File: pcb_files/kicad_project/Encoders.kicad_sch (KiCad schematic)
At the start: 10 parts, among them IC1 AS5145B-HSST, IC2 AS5145B-HSST

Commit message: Finaliza (En principio) el esquematico
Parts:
- removed ENC_1_DAT_CONN1, ENC_2_DAT_CONN1: Conn_01x03_Male, PCB_ZoroBot_v3:Placa_Dat_Encd_Zoro, symbol PCB_ZoroBot_v3-rescue:Conn_01x03_Male-Connector
- removed ENC_1_POT_CONN1, ENC_2_POT_CONN1: Conn_01x02_Male, PCB_ZoroBot_v3:Placa_Pot_Encd_Zoro, symbol PCB_ZoroBot_v3-rescue:Conn_01x02_Male-Connector
- added ENC_D_CONN, ENC_I_CONN: Conn_01x05_Pin, symbol Connector:Conn_01x05_Pin
- renumbered C35 to C23, C36 to C24, C37 to C25, C46 to C31, IC2 to ENC_D1, IC1 to ENC_I1
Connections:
- net ENC_1_3.3 renamed ENC_I_3.3
- net ENC_I_3.3: now also ENC_I_CONN.2 (Pin_2)
- net ENC_1_A_CONN renamed ENC_I_A_CONN
- net ENC_I_A_CONN: now also ENC_I_CONN.3 (Pin_3)
- net ENC_1_B_CONN renamed ENC_I_B_CONN
- net ENC_I_B_CONN: now also ENC_I_CONN.4 (Pin_4)
- net ENC_1_GND renamed ENC_I_GND
- net ENC_I_GND: now also ENC_I_CONN.1 (Pin_1)
- net ENC_1_I_CONN renamed ENC_I_I_CONN
- net ENC_I_I_CONN: now also ENC_I_CONN.5 (Pin_5)
- net ENC_2_3.3 renamed ENC_D_3.3
- net ENC_D_3.3: now also ENC_D_CONN.2 (Pin_2)
- net ENC_2_A_CONN renamed ENC_D_A_CONN
- net ENC_D_A_CONN: now also ENC_D_CONN.3 (Pin_3)
- net ENC_2_B_CONN renamed ENC_D_B_CONN
- net ENC_D_B_CONN: now also ENC_D_CONN.4 (Pin_4)
- net ENC_2_GND renamed ENC_D_GND
- net ENC_D_GND: now also ENC_D_CONN.1 (Pin_1)
- net ENC_2_I_CONN renamed ENC_D_I_CONN
- net ENC_D_I_CONN: now also ENC_D_CONN.5 (Pin_5)
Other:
- note added: "ENCODER MOTOR DERECHO"
- note added: "ENCODER MOTOR IZQUIERDO"
- moved on the sheet: C23, C24, C25, C31, ENC_D1, ENC_I1

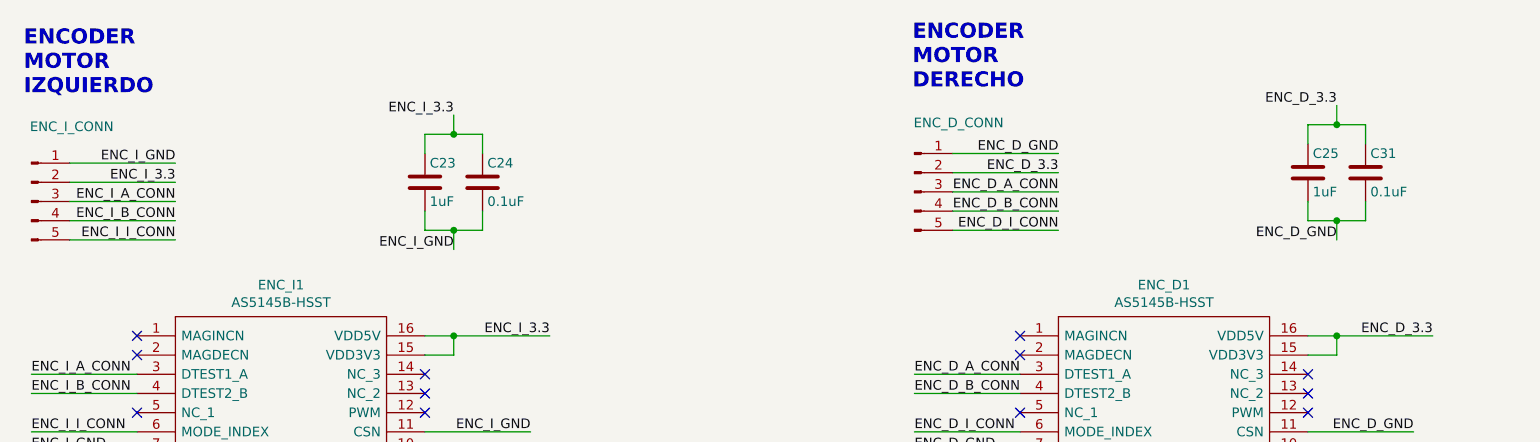
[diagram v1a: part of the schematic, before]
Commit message: Correlaciona toda la NetList, añade EdgeCuts y comienza el posicionamiento de componentes
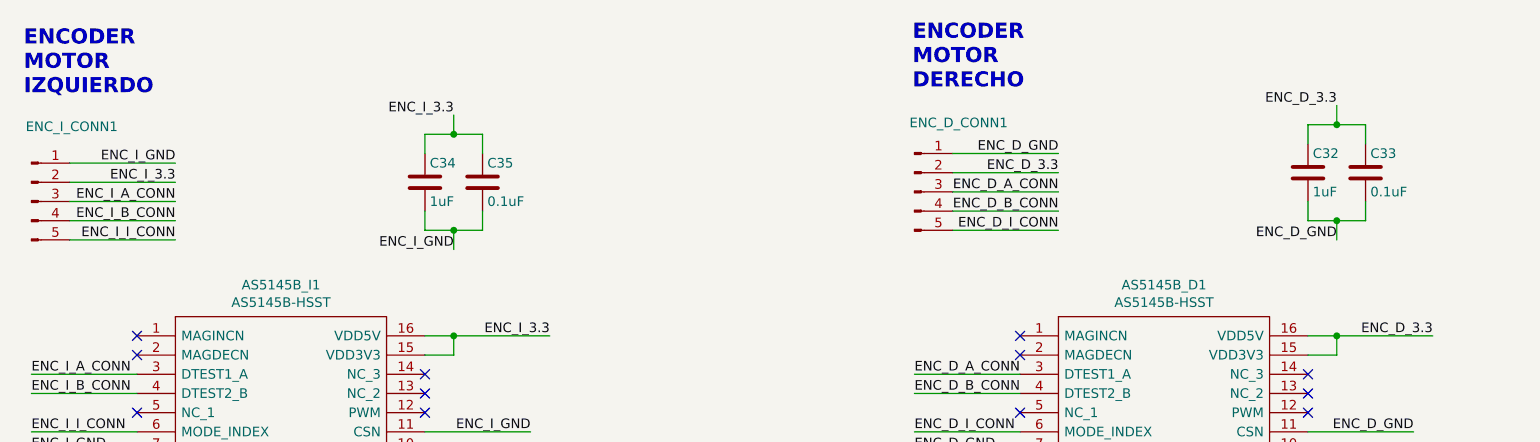
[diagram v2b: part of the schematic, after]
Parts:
- AS5145B_D1: renamed from ENC_D1; footprint AS5145B-HSST:SOP65P780X199-16N -> Package_SO:SSOP-16_5.3x6.2mm_P0.65mm
- AS5145B_I1: renamed from ENC_I1; footprint AS5145B-HSST:SOP65P780X199-16N -> Package_SO:SSOP-20_5.3x7.2mm_P0.65mm
- C32: renamed from C25; footprint Capacitor_SMD:C_0805_2012Metric -> Capacitor_SMD:C_0402_1005Metric_Pad0.74x0.62mm_HandSolder
- C33: renamed from C31; footprint Capacitor_SMD:C_0805_2012Metric -> Capacitor_SMD:C_0402_1005Metric_Pad0.74x0.62mm_HandSolder
- C34: renamed from C23; footprint Capacitor_SMD:C_0805_2012Metric -> Capacitor_SMD:C_0402_1005Metric_Pad0.74x0.62mm_HandSolder
- C35: renamed from C24; footprint Capacitor_SMD:C_0805_2012Metric -> Capacitor_SMD:C_0402_1005Metric_Pad0.74x0.62mm_HandSolder
- ENC_D_CONN1: renamed from ENC_D_CONN; footprint (none) -> custom_footprints:FujitoraBot2_PCBmodule_encoder
- ENC_I_CONN1: renamed from ENC_I_CONN; footprint (none) -> custom_footprints:FujitoraBot2_PCBmodule_encoder
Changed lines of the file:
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@@
 		(on_board yes)
 		(dnp no)
-		(property "Reference" "ENC_I_CONN"
+		(property "Reference" "ENC_I_CONN1"
 			(at 57.404 75.184 0)
 			(effects
@@
 			)
 		)
-		(property "Footprint" ""
+		(property "Footprint" "custom_footprints:FujitoraBot2_PCBmodule_encoder"
 			(at 52.07 85.09 0)
 			(effects
@@
 			(project ""
 				(path "/38e8b839-c362-4120-bbf7-582efa82e48d/fe1aa100-f33c-4fed-9a9a-b5cbbb3bba93"
-					(reference "ENC_I_CONN")
+					(reference "ENC_I_CONN1")
 					(unit 1)
 				)
@@
 		(on_board yes)
 		(dnp no)
-		(property "Reference" "C31"
+		(property "Reference" "C33"
 			(at 229.235 78.74 0)
 			(effects
@@
 			)
 		)
-		(property "Footprint" "Capacitor_SMD:C_0805_2012Metric"
+		(property "Footprint" "Capacitor_SMD:C_0402_1005Metric_Pad0.74x0.62mm_HandSolder"
 			(at 229.5652 85.09 0)
 			(effects
@@
 			(project "ZoroBot3"
 				(path "/38e8b839-c362-4120-bbf7-582efa82e48d/fe1aa100-f33c-4fed-9a9a-b5cbbb3bba93"
-					(reference "C31")
+					(reference "C33")
 					(unit 1)
 				)
@@
 		(on_board yes)
 		(dnp no)
-		(property "Reference" "ENC_I1"
+		(property "Reference" "AS5145B_I1"
 			(at 85.09 96.139 0)
 			(effects
@@
 			)
 		)
-		(property "Footprint" "AS5145B-HSST:SOP65P780X199-16N"
+		(property "Footprint" "Package_SO:SSOP-20_5.3x7.2mm_P0.65mm"
 			(at 100.33 100.33 0)
 			(effects
@@
 			(project "ZoroBot3"
 				(path "/38e8b839-c362-4120-bbf7-582efa82e48d/fe1aa100-f33c-4fed-9a9a-b5cbbb3bba93"
-					(reference "ENC_I1")
+					(reference "AS5145B_I1")
 					(unit 1)
 				)
@@
 		(on_board yes)
 		(dnp no)
-		(property "Reference" "C25"
+		(property "Reference" "C32"
 			(at 221.615 78.74 0)
 			(effects
@@
 			)
 		)
-		(property "Footprint" "Capacitor_SMD:C_0805_2012Metric"
+		(property "Footprint" "Capacitor_SMD:C_0402_1005Metric_Pad0.74x0.62mm_HandSolder"
 			(at 221.9452 85.09 0)
 			(effects
@@
 			(project "ZoroBot3"
 				(path "/38e8b839-c362-4120-bbf7-582efa82e48d/fe1aa100-f33c-4fed-9a9a-b5cbbb3bba93"
-					(reference "C25")
+					(reference "C32")
 					(unit 1)
 				)
@@
 		(on_board yes)
 		(dnp no)
-		(property "Reference" "ENC_D1"
+		(property "Reference" "AS5145B_D1"
 			(at 201.93 96.139 0)
 			(effects
@@
 			)
 		)
-		(property "Footprint" "AS5145B-HSST:SOP65P780X199-16N"
+		(property "Footprint" "Package_SO:SSOP-16_5.3x6.2mm_P0.65mm"
 			(at 217.17 100.33 0)
 			(effects
@@
 			(project "ZoroBot3"
 				(path "/38e8b839-c362-4120-bbf7-582efa82e48d/fe1aa100-f33c-4fed-9a9a-b5cbbb3bba93"
-					(reference "ENC_D1")
+					(reference "AS5145B_D1")
 					(unit 1)
 				)
@@
 		(on_board yes)
 		(dnp no)
-		(property "Reference" "ENC_D_CONN"
+		(property "Reference" "ENC_D_CONN1"
 			(at 174.752 74.676 0)
 			(effects
@@
 			)
 		)
-		(property "Footprint" ""
+		(property "Footprint" "custom_footprints:FujitoraBot2_PCBmodule_encoder"
 			(at 168.91 83.82 0)
 			(effects
@@
 			(project ""
 				(path "/38e8b839-c362-4120-bbf7-582efa82e48d/fe1aa100-f33c-4fed-9a9a-b5cbbb3bba93"
-					(reference "ENC_D_CONN")
+					(reference "ENC_D_CONN1")
 					(unit 1)
 				)
@@
 		(on_board yes)
 		(dnp no)
-		(property "Reference" "C23"
+		(property "Reference" "C34"
 			(at 104.775 80.01 0)
 			(effects
@@
 			)
 		)
-		(property "Footprint" "Capacitor_SMD:C_0805_2012Metric"
+		(property "Footprint" "Capacitor_SMD:C_0402_1005Metric_Pad0.74x0.62mm_HandSolder"
 			(at 105.1052 86.36 0)
 			(effects
@@
 			(project "ZoroBot3"
 				(path "/38e8b839-c362-4120-bbf7-582efa82e48d/fe1aa100-f33c-4fed-9a9a-b5cbbb3bba93"
-					(reference "C23")
+					(reference "C34")
 					(unit 1)
 				)
@@
 		(on_board yes)
 		(dnp no)
-		(property "Reference" "C24"
+		(property "Reference" "C35"
 			(at 112.395 80.01 0)
 			(effects
@@
 			)
 		)
-		(property "Footprint" "Capacitor_SMD:C_0805_2012Metric"
+		(property "Footprint" "Capacitor_SMD:C_0402_1005Metric_Pad0.74x0.62mm_HandSolder"
 			(at 112.7252 86.36 0)
 			(effects
@@
 			(project "ZoroBot3"
 				(path "/38e8b839-c362-4120-bbf7-582efa82e48d/fe1aa100-f33c-4fed-9a9a-b5cbbb3bba93"
-					(reference "C24")
+					(reference "C35")
 					(unit 1)
 				)

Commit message: Corrige errores de esquematico, crea las PCBs auxiliares, y posiciona todos los elementos para comenzar el ruteado.
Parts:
- AS5145B_I1: footprint Package_SO:SSOP-20_5.3x7.2mm_P0.65mm -> Package_SO:SSOP-16_5.3x6.2mm_P0.65mm
- ENC_D_CONN1, ENC_I_CONN1: footprint custom_footprints:FujitoraBot2_PCBmodule_encoder -> custom_footprints:ZoroBot3_PCBmodule_encoder
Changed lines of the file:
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@@
 			)
 		)
-		(property "Footprint" "custom_footprints:FujitoraBot2_PCBmodule_encoder"
+		(property "Footprint" "custom_footprints:ZoroBot3_PCBmodule_encoder"
 			(at 52.07 85.09 0)
 			(effects
@@
 			)
 		)
-		(property "Footprint" "Package_SO:SSOP-20_5.3x7.2mm_P0.65mm"
+		(property "Footprint" "Package_SO:SSOP-16_5.3x6.2mm_P0.65mm"
 			(at 100.33 100.33 0)
 			(effects
@@
 			)
 		)
-		(property "Footprint" "custom_footprints:FujitoraBot2_PCBmodule_encoder"
+		(property "Footprint" "custom_footprints:ZoroBot3_PCBmodule_encoder"
 			(at 168.91 83.82 0)
 			(effects

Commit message: Finaliza el diseño de la PCB de ZoroBot3 Rebuild y añade gerbers y BOM
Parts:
- AS5145B_D1, AS5145B_I1: footprint Package_SO:SSOP-16_5.3x6.2mm_P0.65mm -> custom_footprints:Encoder_AS5145B
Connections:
- net ENC_D_A_CONN: now also ENC_D_CONN1.4 (Pin_4); no longer ENC_D_CONN1.3 (Pin_3)
- net ENC_D_B_CONN: now also ENC_D_CONN1.5 (Pin_5); no longer ENC_D_CONN1.4 (Pin_4)
- net ENC_D_I_CONN: now also ENC_D_CONN1.3 (Pin_3); no longer ENC_D_CONN1.5 (Pin_5)
- net ENC_I_A_CONN: now also ENC_I_CONN1.4 (Pin_4); no longer ENC_I_CONN1.3 (Pin_3)
- net ENC_I_B_CONN: now also ENC_I_CONN1.5 (Pin_5); no longer ENC_I_CONN1.4 (Pin_4)
- net ENC_I_I_CONN: now also ENC_I_CONN1.3 (Pin_3); no longer ENC_I_CONN1.5 (Pin_5)
